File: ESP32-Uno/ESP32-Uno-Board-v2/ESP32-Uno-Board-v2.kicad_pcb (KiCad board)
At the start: 2 copper layers, 68.8 x 53.2 mm, 19 parts, among them J1 USB-C_Receptacle_Data_16P_GCT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, J2 Barrel_Jack_Switch, Q1 DMP6180SK3, SW1 SW_SPDT, SW2 SW_Push_SMD_6x3.5, U1 ESP32-S3-WROOM-1, U2 LM1117MP-3.3, U3 AMS1117-5V

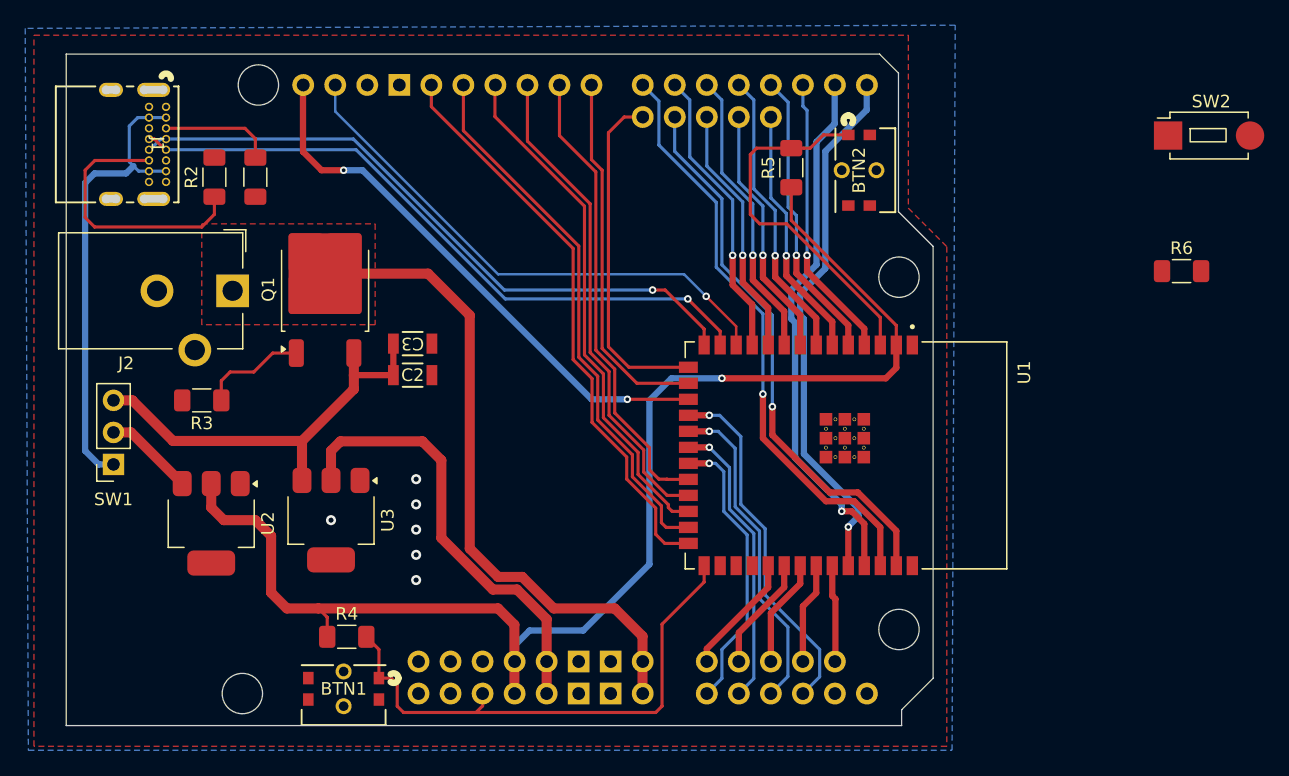
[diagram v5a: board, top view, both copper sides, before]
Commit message: ESP32-Uno
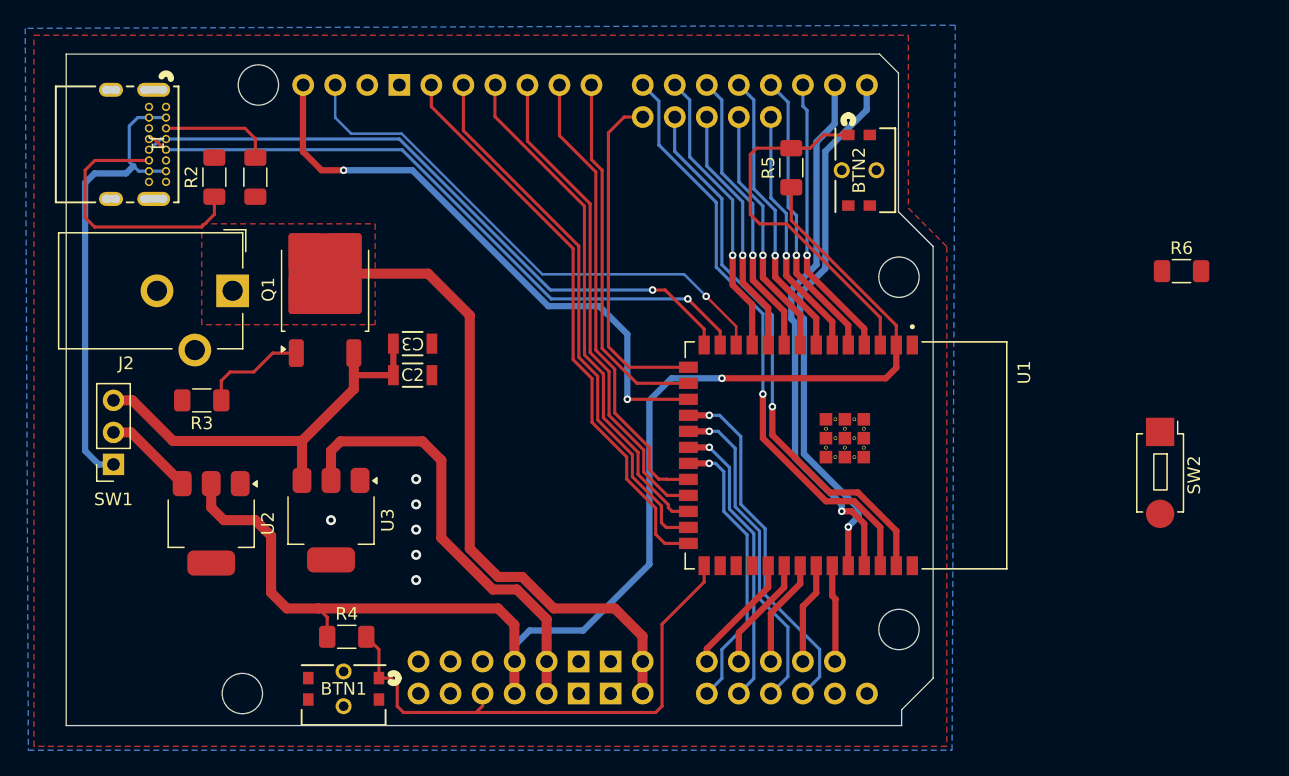
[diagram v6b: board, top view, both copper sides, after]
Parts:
- moved SW2 23.5 mm to (196.8, 129.5), turned to -90 degrees
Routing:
- net /SCL: track 43.9 -> 46.9 mm
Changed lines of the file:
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@@
 	(footprint "Alexander Footprint Library:SW_PUSH_6x3.5mm"
 		(layer "F.Cu")
-		(at 197.38 106)
+		(at 196.75 129.5 -90)
 		(descr "tactile push button, 6x3.5mm, https://www.apem.com/idec-apem/en_US/PCB-switches/Tactile-Switches/MJTP-6mm-through-hole/c/MJTP_6mm_through%20hole?page=1")
 		(tags "PHAP3362 6mm tact sw THT")
 		(property "Reference" "SW2"
-			(at 3.42 -2.7 0)
+			(at 3.42 -2.7 90)
 			(layer "F.SilkS")
 			(effects
@@
 		)
 		(property "Value" "SW_Push_SMD_6x3.5"
-			(at 4.4 3.7 0)
+			(at 4.4 3.7 90)
 			(layer "F.Fab")
 			(effects
@@
 		)
 		(property "Footprint" "Alexander Footprint Library:SW_PUSH_6x3.5mm"
-			(at 0 0 0)
+			(at 0 0 -90)
 			(unlocked yes)
 			(layer "F.Fab")
@@
 		)
 		(property "Datasheet" ""
-			(at 0 0 0)
+			(at 0 0 -90)
 			(unlocked yes)
 			(layer "F.Fab")
@@
 		)
 		(property "Description" ""
-			(at 0 0 0)
+			(at 0 0 -90)
 			(unlocked yes)
 			(layer "F.Fab")
@@
 		(attr through_hole)
 		(fp_line
-			(start 0.15 -1.85)
-			(end 0.15 -1.39)
+			(start 0.15 1.85)
+			(end 6.35 1.85)
 			(stroke
 				(width 0.12)
-				(type default)
+				(type solid)
 			)
 			(layer "F.SilkS")
 		)
 		(fp_line
-			(start 0.15 -1.39)
-			(end -0.85 -1.39)
+			(start 0.15 1.39)
+			(end 0.15 1.85)
 			(stroke
 				(width 0.12)
-				(type default)
+				(type solid)
 			)
 			(layer "F.SilkS")
 		)
 		(fp_line
-			(start 0.15 1.39)
-			(end 0.15 1.85)
+			(start 6.35 1.39)
+			(end 6.35 1.85)
 			(stroke
 				(width 0.12)
@@
 		)
 		(fp_line
-			(start 0.15 1.85)
-			(end 6.35 1.85)
+			(start 0.15 -1.39)
+			(end -0.85 -1.39)
 			(stroke
 				(width 0.12)
-				(type solid)
+				(type default)
 			)
 			(layer "F.SilkS")
 		)
 		(fp_line
-			(start 6.35 -1.85)
-			(end 0.15 -1.85)
+			(start 0.15 -1.85)
+			(end 0.15 -1.39)
 			(stroke
 				(width 0.12)
-				(type solid)
+				(type default)
 			)
 			(layer "F.SilkS")
@@
 		)
 		(fp_line
-			(start 6.35 1.39)
-			(end 6.35 1.85)
+			(start 6.35 -1.85)
+			(end 0.15 -1.85)
 			(stroke
 				(width 0.12)
@@
 		)
 		(fp_line
-			(start -1.38 -1.38)
-			(end 0 -1.38)
+			(start 6.5 2)
+			(end 0 2)
 			(stroke
 				(width 0.05)
-				(type default)
+				(type solid)
 			)
 			(layer "F.CrtYd")
@@
 		(fp_line
 			(start -1.38 1.38)
-			(end -1.38 -1.38)
+			(end 0 1.38)
 			(stroke
 				(width 0.05)
-				(type solid)
+				(type default)
 			)
 			(layer "F.CrtYd")
@@
 		(fp_line
 			(start -1.38 1.38)
-			(end 0 1.38)
+			(end -1.38 -1.38)
 			(stroke
 				(width 0.05)
-				(type default)
+				(type solid)
 			)
 			(layer "F.CrtYd")
 		)
 		(fp_line
-			(start 0 -2)
-			(end 0 -1.38)
+			(start 0 1.38)
+			(end 0 2)
 			(stroke
 				(width 0.05)
@@
 		)
 		(fp_line
-			(start 0 -2)
-			(end 6.5 -2)
+			(start 6.5 1.38)
+			(end 6.5 2)
 			(stroke
 				(width 0.05)
-				(type solid)
+				(type default)
 			)
 			(layer "F.CrtYd")
 		)
 		(fp_line
-			(start 0 1.38)
-			(end 0 2)
+			(start -1.38 -1.38)
+			(end 0 -1.38)
 			(stroke
 				(width 0.05)
@@
 		)
 		(fp_line
-			(start 6.5 -2)
-			(end 6.5 -1.38)
+			(start 0 -2)
+			(end 0 -1.38)
 			(stroke
 				(width 0.05)
@@
 		)
 		(fp_line
-			(start 6.5 1.38)
-			(end 6.5 2)
+			(start 0 -2)
+			(end 6.5 -2)
 			(stroke
 				(width 0.05)
-				(type default)
+				(type solid)
 			)
 			(layer "F.CrtYd")
 		)
 		(fp_line
-			(start 6.5 2)
-			(end 0 2)
+			(start 6.5 -2)
+			(end 6.5 -1.38)
 			(stroke
 				(width 0.05)
-				(type solid)
+				(type default)
 			)
 			(layer "F.CrtYd")
@@
 		)
 		(fp_line
-			(start 0.65 -1.75)
-			(end 0.25 -1.35)
+			(start 6.25 1.75)
+			(end 0.25 1.75)
 			(stroke
 				(width 0.1)
-				(type default)
+				(type solid)
 			)
 			(layer "F.Fab")
@@
 		(fp_line
 			(start 0.65 -1.75)
-			(end 6.25 -1.75)
+			(end 0.25 -1.35)
 			(stroke
 				(width 0.1)
-				(type solid)
+				(type default)
 			)
 			(layer "F.Fab")
 		)
 		(fp_line
-			(start 6.25 -1.75)
-			(end 6.25 1.75)
+			(start 0.65 -1.75)
+			(end 6.25 -1.75)
 			(stroke
 				(width 0.1)
@@
 		)
 		(fp_line
-			(start 6.25 1.75)
-			(end 0.25 1.75)
+			(start 6.25 -1.75)
+			(end 6.25 1.75)
 			(stroke
 				(width 0.1)
@@
 		)
 		(fp_text user "${REFERENCE}"
-			(at 3 0 0)
+			(at 3 0 90)
 			(layer "F.Fab")
 			(effects
@@
 		)
 		(pad "1" smd rect
-			(at 0 0 90)
+			(at 0 0)
 			(size 2.25 2.25)
 			(layers "F.Cu" "F.Paste" "F.Mask")
@@
 		)
 		(pad "2" smd oval
-			(at 6.5 0 90)
+			(at 6.5 0)
 			(size 2.25 2.25)
 			(layers "F.Cu" "F.Paste" "F.Mask")
@@
 	)
 	(segment
-		(start 117.494159 106.274444)
-		(end 116.644158 107.124445)
+		(start 148.39896 118.25)
+		(end 136.423404 106.274444)
 		(width 0.25)
 		(layer "B.Cu")
@@
 	)
 	(segment
-		(start 132.774444 106.274444)
-		(end 117.917566 106.274444)
+		(start 117.494159 106.274444)
+		(end 116.644158 107.124445)
 		(width 0.25)
 		(layer "B.Cu")
@@
 	)
 	(segment
-		(start 144.75 118.25)
-		(end 132.774444 106.274444)
+		(start 156.5 118.25)
+		(end 148.39896 118.25)
 		(width 0.25)
 		(layer "B.Cu")
@@
 	)
 	(segment
-		(start 116.644158 107.124445)
-		(end 116.567566 107.124445)
+		(start 136.423404 106.274444)
+		(end 117.917566 106.274444)
 		(width 0.25)
 		(layer "B.Cu")
@@
 	)
 	(segment
-		(start 156.5 118.25)
-		(end 144.75 118.25)
+		(start 116.644158 107.124445)
+		(end 116.567566 107.124445)
 		(width 0.25)
 		(layer "B.Cu")
@@
 	)
 	(segment
-		(start 132.988049 107.124445)
+		(start 136.637009 107.124445)
 		(end 117.917566 107.124445)
 		(width 0.25)
@@
 	)
 	(segment
-		(start 144.818604 118.955)
-		(end 132.988049 107.124445)
+		(start 159.295 118.955)
+		(end 148.467564 118.955)
 		(width 0.25)
 		(layer "B.Cu")
@@
 	)
 	(segment
-		(start 159.295 118.955)
-		(end 144.818604 118.955)
+		(start 148.467564 118.955)
+		(end 136.637009 107.124445)
 		(width 0.25)
 		(layer "B.Cu")
@@
 	)
 	(segment
-		(start 159 117)
-		(end 144.25 117)
+		(start 160.75 118.75)
+		(end 159 117)
 		(width 0.2)
 		(layer "B.Cu")
@@
 	)
 	(segment
-		(start 160.75 118.75)
-		(end 159 117)
+		(start 147.75 117)
+		(end 136.599444 105.849444)
 		(width 0.2)
 		(layer "B.Cu")
@@
 	)
 	(segment
-		(start 131.336 104.086)
-		(end 131.336 101.99)
+		(start 136.599444 105.849444)
+		(end 132.599444 105.849444)
+		(width 0.2)
+		(layer "B.Cu")
+		(net 49)
+	)
+	(segment
+		(start 159 117)
+		(end 147.75 117)
 		(width 0.2)
 		(layer "B.Cu")
@@
 	)
 	(segment
-		(start 144.25 117)
-		(end 131.336 104.086)
+		(start 132.599444 105.849444)
+		(end 131.336 104.586)
+		(width 0.2)
+		(layer "B.Cu")
+		(net 49)
+	)
+	(segment
+		(start 131.336 104.586)
+		(end 131.336 101.99)
 		(width 0.2)
 		(layer "B.Cu")
@@
 	)
 	(segment
-		(start 151.665 126.915)
-		(end 133.5 108.75)
+		(start 152.28 119.53)
+		(end 148.229391 119.53)
 		(width 0.5)
 		(layer "B.Cu")
@@
 	)
 	(segment
-		(start 133.5 108.75)
-		(end 132 108.75)
+		(start 154.5 121.75)
+		(end 152.28 119.53)
 		(width 0.5)
 		(layer "B.Cu")
@@
 	(segment
 		(start 154.5 126.915)
-		(end 151.665 126.915)
+		(end 154.5 121.75)
+		(width 0.5)
+		(layer "B.Cu")
+		(net 50)
+	)
+	(segment
+		(start 148.229391 119.53)
+		(end 137.449391 108.75)
+		(width 0.5)
+		(layer "B.Cu")
+		(net 50)
+	)
+	(segment
+		(start 137.449391 108.75)
+		(end 132 108.75)
 		(width 0.5)
 		(layer "B.Cu")

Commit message: ESP32-Uno
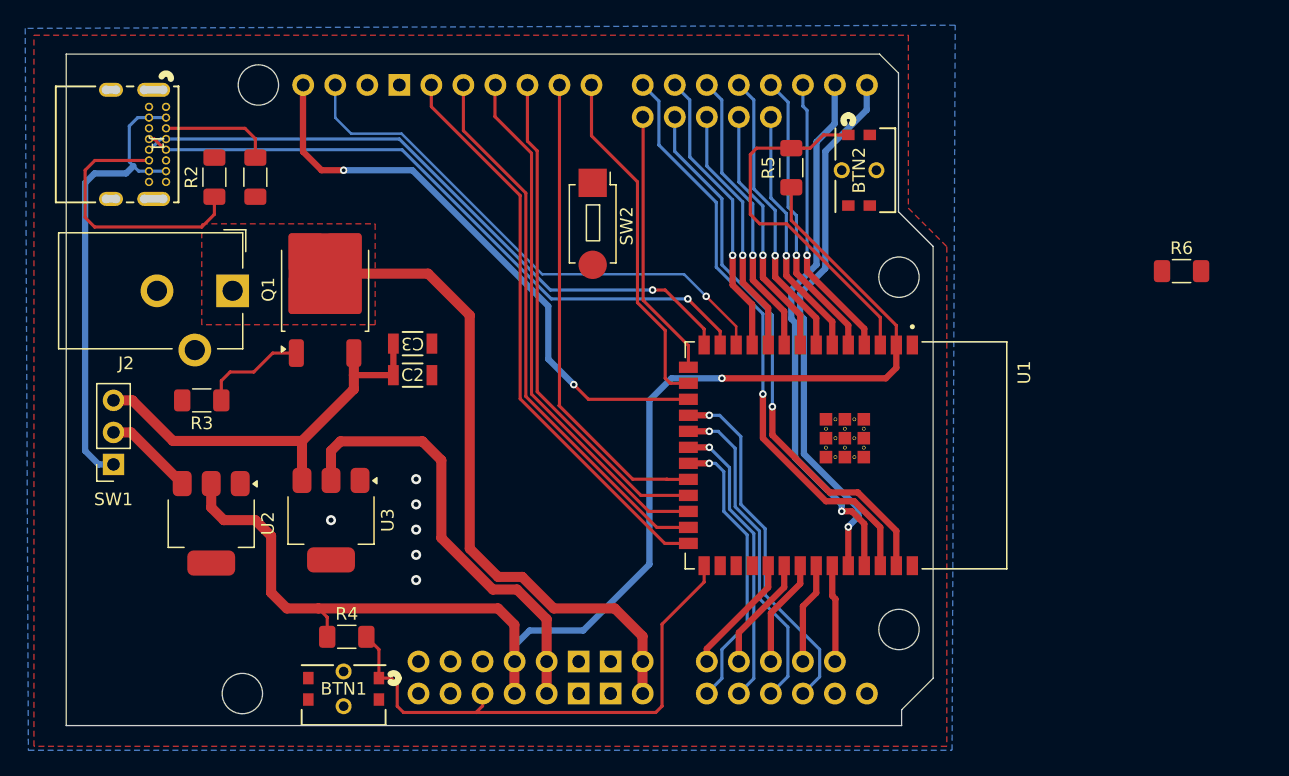
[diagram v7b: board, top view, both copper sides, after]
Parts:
- moved SW2 49.1 mm to (151.8, 109.8)
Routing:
- net /GPIO3: track 27.2 -> 21.3 mm
- net /GPIO46: track 29.2 -> 27.7 mm
- net /GPIO14: track 36.9 -> 38.1 mm
- net /GPIO21: track 38.8 -> 40.0 mm
- net /GPIO47: track 40.9 -> 42.0 mm
- net /SCL: track 46.9 -> 46.3 mm
